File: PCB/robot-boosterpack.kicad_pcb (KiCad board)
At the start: 2 copper layers, 58.4 x 73.7 mm, 57 parts, among them IC1 DRV8833, IC2 TPS77033, IC3 TPS77050, IC4 LMR61428, J1 3.3V Jumper, J2 5V Jumper, J3 9V Jumper, M1 MOTOR, M2 MOTOR

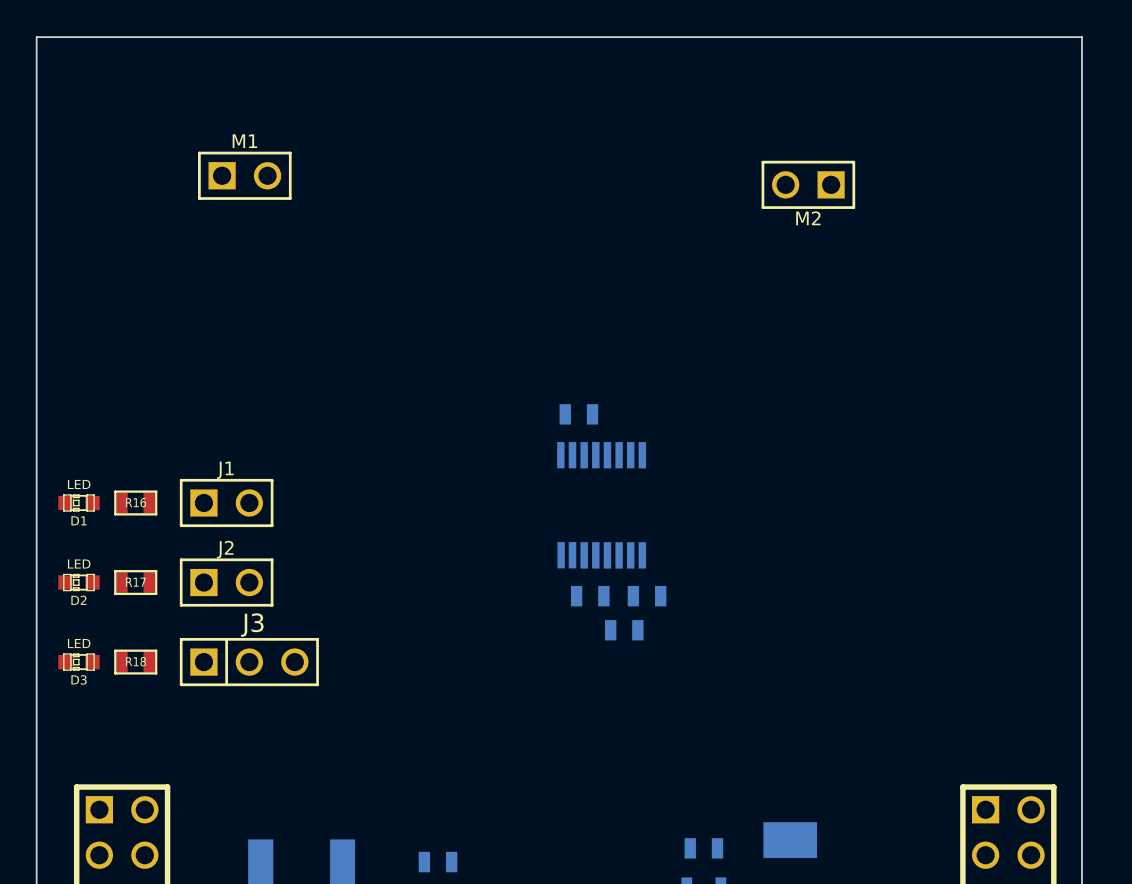
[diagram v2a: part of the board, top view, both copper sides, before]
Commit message: added motor mount drill holes
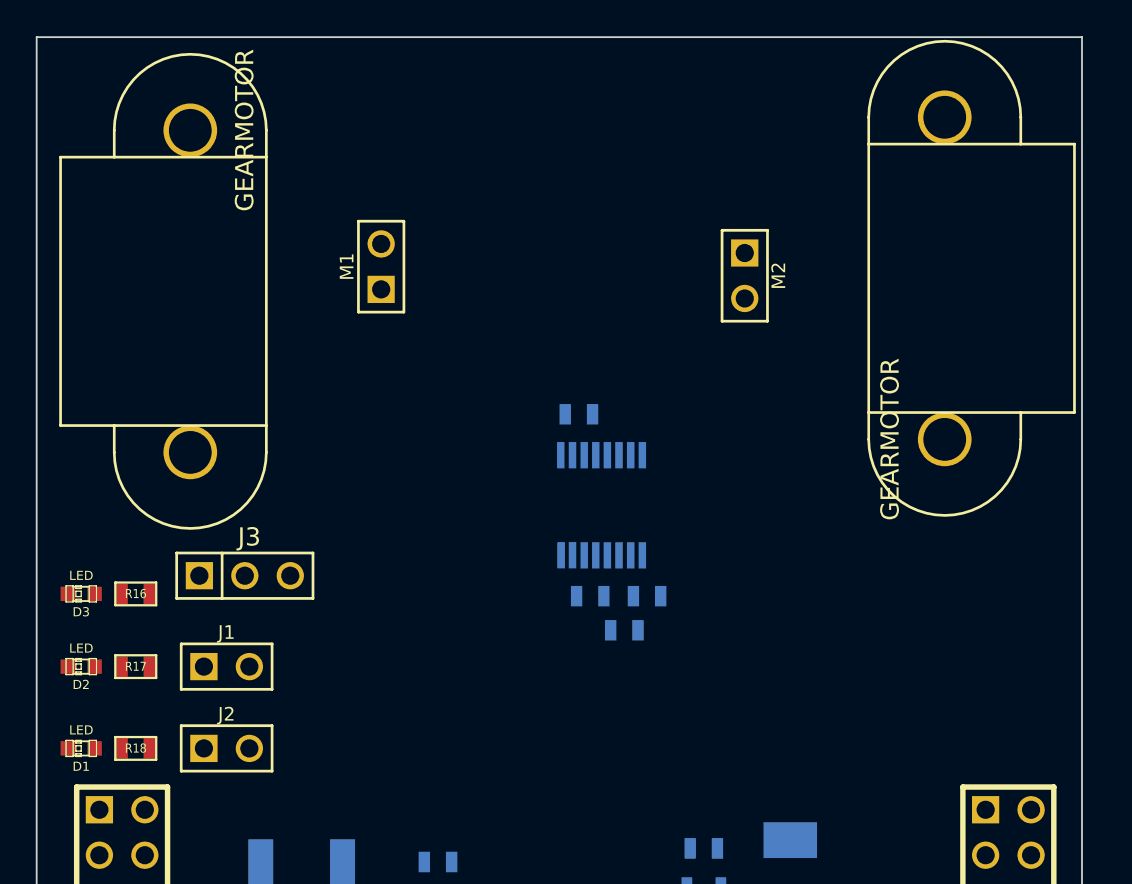
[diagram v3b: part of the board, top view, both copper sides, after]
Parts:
- added GEARMOTOR: P***, 1pin, F.Cu at (177.8, 70.6)
- added GEARMOTOR: P***, 1pin, F.Cu at (220.0, 87.9)
- moved D1 13.7 mm to (171.7, 105.2)
- moved J2 9.27 mm to (179.8, 105.2)
- moved M1 9.16 mm to (188.5, 78.2), turned to 90 degrees
- moved J1 9.14 mm to (179.8, 100.6)
- moved M2 6.20 mm to (208.8, 78.7), turned to 270 degrees
- moved R16 5.08 mm to (174.8, 96.5)
- moved J3 4.83 mm to (180.8, 95.5)
- moved R18 4.83 mm to (174.8, 105.2)
- moved D2 4.70 mm to (171.7, 100.6)
- moved R17 4.70 mm to (174.8, 100.6)
- moved D3 3.81 mm to (171.7, 96.5)
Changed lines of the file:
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@@
     (links 120)
     (no_connects 120)
-    (area 26.270227 24.870834 228.1936 139.115001)
+    (area 169.164999 65.354999 228.1936 161.571001)
     (thickness 1.6)
     (drawings 4)
     (tracks 0)
     (zones 0)
-    (modules 57)
+    (modules 59)
     (nets 40)
   )
@@
     (mod_text_size 1 1)
     (mod_text_width 0.15)
-    (pad_size 1.5 1.5)
-    (pad_drill 0.6)
+    (pad_size 3 3)
+    (pad_drill 2.39)
     (pad_to_mask_clearance 0)
     (aux_axis_origin 0 0)
@@
     (add_net N-000008)
   )
+  (module 1pin (layer F.Cu)
+    (at 177.8 70.612 270)
+    (descr "module 1 pin (ou trou mecanique de percage)")
+    (tags DEV)
+    (path 1pin)
+    (fp_text reference GEARMOTOR (at 0 -3.048 270) (layer F.SilkS)
+      (effects (font (size 1.016 1.016) (thickness 0.254)))
+    )
+    (fp_text value P*** (at 0 2.794 270) (layer F.SilkS) hide
+      (effects (font (size 1.016 1.016) (thickness 0.254)))
+    )
+    (fp_line (start 16.5 4.25) (end 18 4.25) (layer F.SilkS) (width 0.15))
+    (fp_line (start 0 4.25) (end 1.5 4.25) (layer F.SilkS) (width 0.15))
+    (fp_line (start 1.5 7.25) (end 1.5 -4.25) (layer F.SilkS) (width 0.15))
+    (fp_line (start 16.5 -4.25) (end 16.5 7.25) (layer F.SilkS) (width 0.15))
+    (fp_line (start 1.5 7.25) (end 16.5 7.25) (layer F.SilkS) (width 0.15))
+    (fp_line (start 0 -4.25) (end 18 -4.25) (layer F.SilkS) (width 0.15))
+    (fp_arc (start 18 0) (end 18 -4.25) (angle 180) (layer F.SilkS) (width 0.15))
+    (fp_arc (start 0 0) (end 0 4.25) (angle 180) (layer F.SilkS) (width 0.15))
+    (pad 1 thru_hole circle (at 0 0 270) (size 3 3) (drill 2.39)
+      (layers *.Cu *.Mask F.SilkS)
+    )
+    (pad 2 thru_hole circle (at 18 0 270) (size 3 3) (drill 2.39)
+      (layers *.Cu *.Mask F.SilkS)
+    )
+  )
+  (module 1pin (layer F.Cu)
+    (at 219.964 87.884 90)
+    (descr "module 1 pin (ou trou mecanique de percage)")
+    (tags DEV)
+    (path 1pin)
+    (fp_text reference GEARMOTOR (at 0 -3.048 90) (layer F.SilkS)
+      (effects (font (size 1.016 1.016) (thickness 0.254)))
+    )
+    (fp_text value P*** (at 0 2.794 90) (layer F.SilkS) hide
+      (effects (font (size 1.016 1.016) (thickness 0.254)))
+    )
+    (fp_line (start 16.5 4.25) (end 18 4.25) (layer F.SilkS) (width 0.15))
+    (fp_line (start 0 4.25) (end 1.5 4.25) (layer F.SilkS) (width 0.15))
+    (fp_line (start 1.5 7.25) (end 1.5 -4.25) (layer F.SilkS) (width 0.15))
+    (fp_line (start 16.5 -4.25) (end 16.5 7.25) (layer F.SilkS) (width 0.15))
+    (fp_line (start 1.5 7.25) (end 16.5 7.25) (layer F.SilkS) (width 0.15))
+    (fp_line (start 0 -4.25) (end 18 -4.25) (layer F.SilkS) (width 0.15))
+    (fp_arc (start 18 0) (end 18 -4.25) (angle 180) (layer F.SilkS) (width 0.15))
+    (fp_arc (start 0 0) (end 0 4.25) (angle 180) (layer F.SilkS) (width 0.15))
+    (pad 1 thru_hole circle (at 0 0 90) (size 3 3) (drill 2.39)
+      (layers *.Cu *.Mask F.SilkS)
+    )
+    (pad 2 thru_hole circle (at 18 0 90) (size 3 3) (drill 2.39)
+      (layers *.Cu *.Mask F.SilkS)
+    )
+  )
   (module tssop-16 (layer B.Cu)
     (at 200.787 91.567)
@@
   )
   (module SM0603 (layer F.Cu)
-    (at 174.752 100.33)
+    (at 174.752 105.156)
     (attr smd)
     (fp_text reference R18 (at 0 0) (layer F.SilkS)
@@
   )
   (module SM0603 (layer F.Cu)
-    (at 174.752 91.44)
+    (at 174.752 96.52)
     (attr smd)
     (fp_text reference R16 (at 0 0) (layer F.SilkS)
@@
   )
   (module SM0603 (layer F.Cu)
-    (at 174.752 95.885)
+    (at 174.752 100.584)
     (attr smd)
     (fp_text reference R17 (at 0 0) (layer F.SilkS)
@@
   )
   (module PIN_ARRAY_3X1 (layer F.Cu)
-    (at 181.102 100.33)
+    (at 180.848 95.504)
     (descr "Connecteur 3 pins")
     (tags "CONN DEV")
@@
   )
   (module PIN_ARRAY_2X1 (layer F.Cu)
-    (at 179.832 95.885)
+    (at 179.832 105.156)
     (descr "Connecteurs 2 pins")
     (tags "CONN DEV")
@@
   )
   (module PIN_ARRAY_2X1 (layer F.Cu)
-    (at 180.848 73.152)
+    (at 188.468 78.232 90)
     (descr "Connecteurs 2 pins")
     (tags "CONN DEV")
-    (fp_text reference M1 (at 0 -1.905) (layer F.SilkS)
+    (fp_text reference M1 (at 0 -1.905 90) (layer F.SilkS)
       (effects (font (size 0.762 0.762) (thickness 0.1524)))
     )
-    (fp_text value MOTOR (at 0 -1.905) (layer F.SilkS) hide
+    (fp_text value MOTOR (at 0 -1.905 90) (layer F.SilkS) hide
       (effects (font (size 0.762 0.762) (thickness 0.1524)))
     )
@@
     (fp_line (start 2.54 -1.27) (end 2.54 1.27) (layer F.SilkS) (width 0.1524))
     (fp_line (start 2.54 1.27) (end -2.54 1.27) (layer F.SilkS) (width 0.1524))
-    (pad 1 thru_hole rect (at -1.27 0) (size 1.524 1.524) (drill 1.016)
+    (pad 1 thru_hole rect (at -1.27 0 90) (size 1.524 1.524) (drill 1.016)
       (layers *.Cu *.Mask F.SilkS)
       (net 37 N-0000059)
     )
-    (pad 2 thru_hole circle (at 1.27 0) (size 1.524 1.524) (drill 1.016)
+    (pad 2 thru_hole circle (at 1.27 0 90) (size 1.524 1.524) (drill 1.016)
       (layers *.Cu *.Mask F.SilkS)
       (net 36 N-0000058)
@@
   )
   (module PIN_ARRAY_2X1 (layer F.Cu)
-    (at 212.344 73.66 180)
+    (at 208.788 78.74 270)
     (descr "Connecteurs 2 pins")
     (tags "CONN DEV")
-    (fp_text reference M2 (at 0 -1.905 180) (layer F.SilkS)
+    (fp_text reference M2 (at 0 -1.905 270) (layer F.SilkS)
       (effects (font (size 0.762 0.762) (thickness 0.1524)))
     )
-    (fp_text value MOTOR (at 0 -1.905 180) (layer F.SilkS) hide
+    (fp_text value MOTOR (at 0 -1.905 270) (layer F.SilkS) hide
       (effects (font (size 0.762 0.762) (thickness 0.1524)))
     )
@@
     (fp_line (start 2.54 -1.27) (end 2.54 1.27) (layer F.SilkS) (width 0.1524))
     (fp_line (start 2.54 1.27) (end -2.54 1.27) (layer F.SilkS) (width 0.1524))
-    (pad 1 thru_hole rect (at -1.27 0 180) (size 1.524 1.524) (drill 1.016)
+    (pad 1 thru_hole rect (at -1.27 0 270) (size 1.524 1.524) (drill 1.016)
       (layers *.Cu *.Mask F.SilkS)
       (net 34 N-0000056)
     )
-    (pad 2 thru_hole circle (at 1.27 0 180) (size 1.524 1.524) (drill 1.016)
+    (pad 2 thru_hole circle (at 1.27 0 270) (size 1.524 1.524) (drill 1.016)
       (layers *.Cu *.Mask F.SilkS)
       (net 35 N-0000057)
@@
   )
   (module PIN_ARRAY_2X1 (layer F.Cu)
-    (at 179.832 91.44)
+    (at 179.832 100.584)
     (descr "Connecteurs 2 pins")
     (tags "CONN DEV")
@@
   )
   (module LED-0603 (layer F.Cu)
-    (at 171.577 91.44 180)
+    (at 171.704 105.156 180)
     (descr "LED 0603 smd package")
     (tags "LED led 0603 SMD smd SMT smt smdled SMDLED smtled SMTLED")
@@
   )
   (module LED-0603 (layer F.Cu)
-    (at 171.577 95.885 180)
+    (at 171.704 100.584 180)
     (descr "LED 0603 smd package")
     (tags "LED led 0603 SMD smd SMT smt smdled SMDLED smtled SMTLED")
@@
   )
   (module LED-0603 (layer F.Cu)
-    (at 171.577 100.33 180)
+    (at 171.704 96.52 180)
     (descr "LED 0603 smd package")
     (tags "LED led 0603 SMD smd SMT smt smdled SMDLED smtled SMTLED")

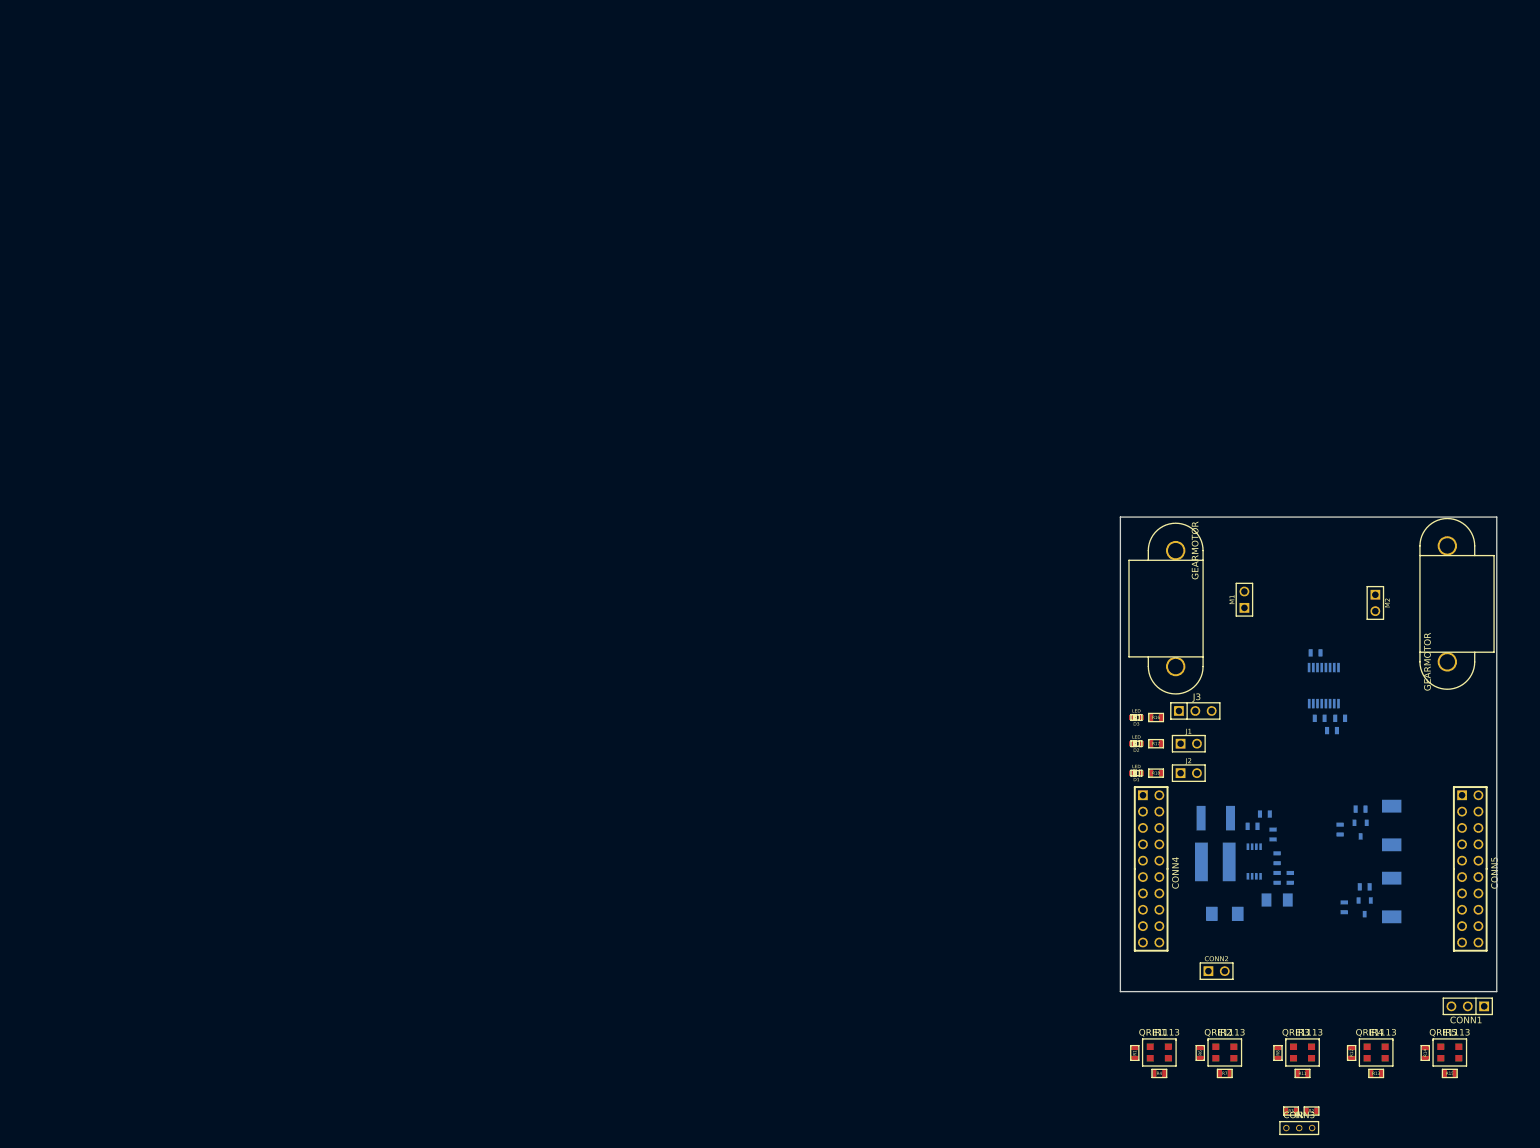
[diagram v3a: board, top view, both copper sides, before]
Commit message: made pcb edges align to 10mm grid
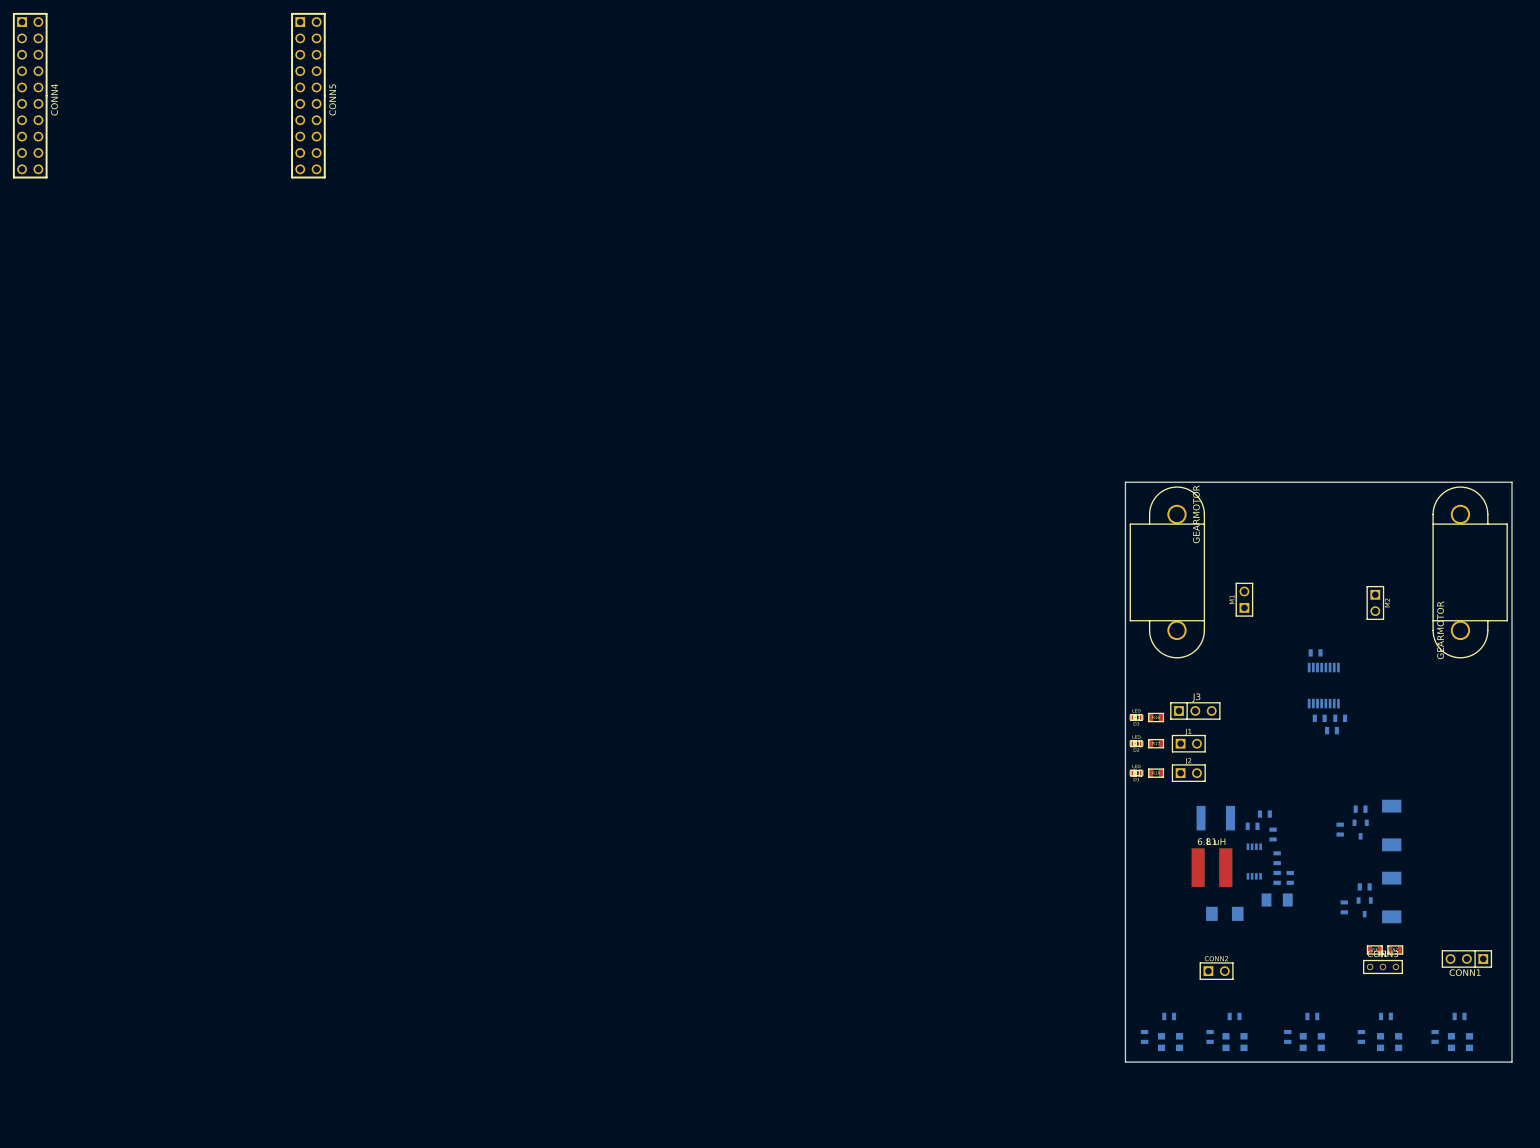
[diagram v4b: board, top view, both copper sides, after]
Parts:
- IR1, IR2, IR3, IR4, IR5, R1, R11, R12, R13, R14, R15, R4, R6, R7, R8: moved to B.Cu
- L1: moved to F.Cu
- moved CONN5 216.6 mm to (43.2, 0.00)
- moved CONN4 211.4 mm to (0.00, 0.00)
- moved CONN3 28.2 mm to (210.0, 133.2)
- moved R2 28.2 mm to (211.9, 132.6)
- moved R3 28.2 mm to (208.7, 132.6)
- moved R13 8.97 mm to (210.4, 142.9)
- moved R15 8.97 mm to (221.9, 142.9)
- moved R4 8.97 mm to (176.8, 142.9)
- moved R7 8.97 mm to (186.9, 142.9)
- moved R11 8.97 mm to (199.0, 142.9)
- moved CONN1 7.35 mm to (223.0, 134.0)
- moved L1 7.13 mm to (183.4, 115.8)
- moved GEARMOTOR 5.62 mm to (178.0, 65.0)
- moved GEARMOTOR 5.29 mm to (222.0, 83.0)
- moved IR4 5.04 mm to (211.0, 150.0)
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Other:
- board size 58.4 x 73.7 mm -> 60 x 90 mm
